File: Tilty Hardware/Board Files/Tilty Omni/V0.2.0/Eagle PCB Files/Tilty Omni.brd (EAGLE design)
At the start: 38.1 x 50.8 mm, 11 parts, among them U1 TEENSY_3.0_ALLPINS

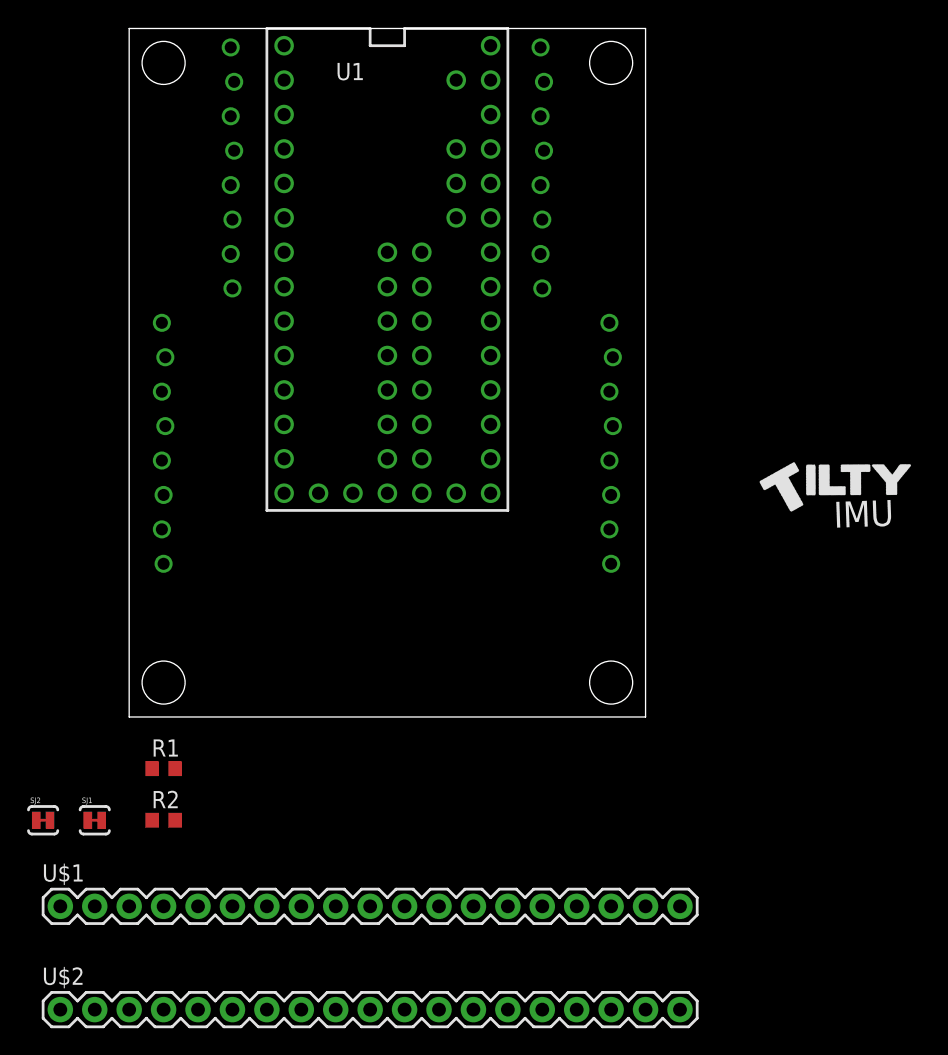
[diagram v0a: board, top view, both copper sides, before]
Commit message: Updated Tilty Omni pinout and removed Eagle backup files,as that's what GitHub is for
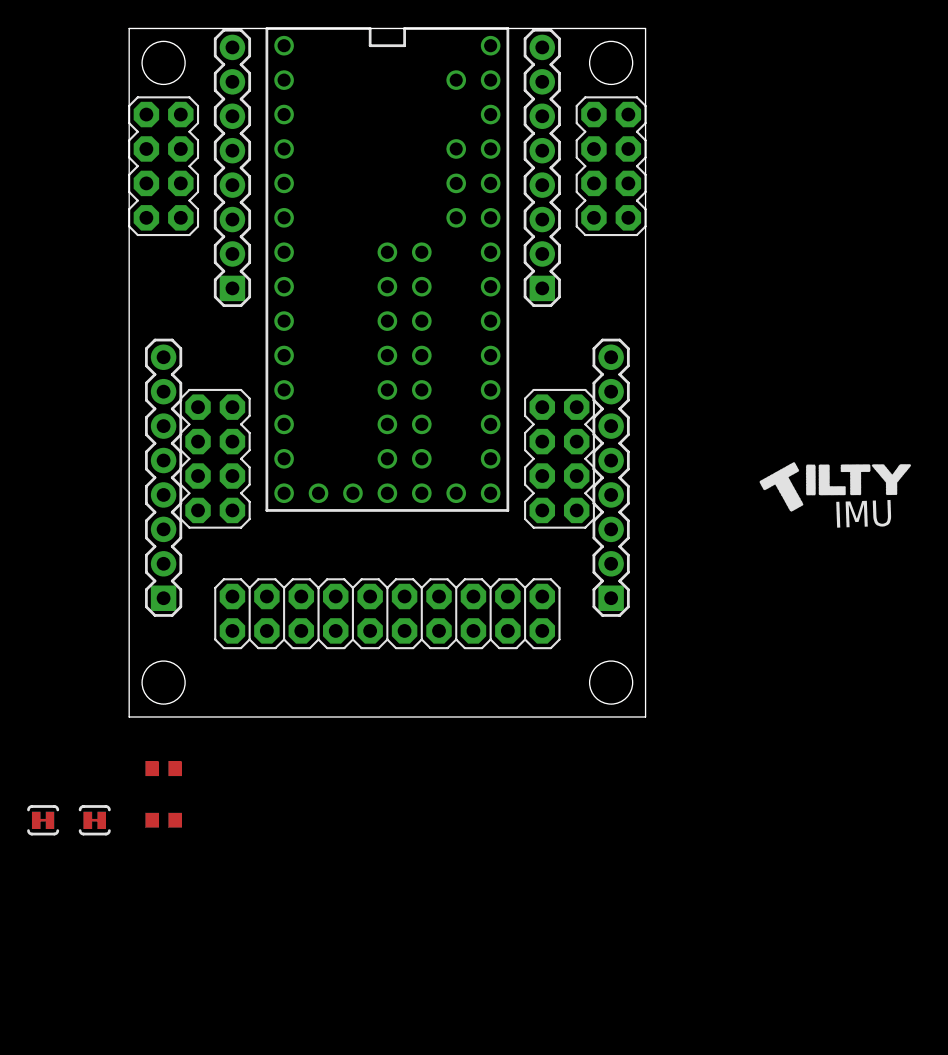
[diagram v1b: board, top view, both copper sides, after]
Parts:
- removed U$1, U$2: M191X19, SparkFun-Connectors:1X19
- added JP10: M10X2, SparkFun-Connectors:2X10
- added JP5, JP6, JP7, JP8: M04X2, SparkFun-Connectors:2X4
- JP1, JP2, JP3, JP4: value 8-PIN_HEADER -> (none); device My Parts:8-PIN_RECEPTACLE_LOCK_NO-SS -> SparkFun-Connectors:1X08
- moved JP2 11.4 mm to (2.54, 8.76), turned to 90 degrees
- moved JP3 11.4 mm to (35.6, 8.76), turned to 90 degrees
- moved JP1 8.89 mm to (7.62, 31.6), turned to 90 degrees
- moved JP4 8.89 mm to (30.5, 31.6), turned to 90 degrees
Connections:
- net N$14 renamed A13
- removed net N$1: U1.24
- removed net N$10: U1.33
- removed net N$2: U1.25
- removed net N$3: U1.26
- removed net N$4: U1.27
- removed net N$5: U1.28
- removed net N$6: U1.29
- removed net N$7: U1.30
- removed net N$8: U1.31
- removed net N$9: U1.32
- new net 24: JP10.10, U1.24
- new net 25: JP10.9, U1.25
- new net 26: JP10.8, U1.26
- new net 27: JP10.7, U1.27
- new net 28: JP10.6, U1.28
- new net 29: JP10.5, U1.29
- new net 30: JP10.4, U1.30
- new net 31: JP10.3, U1.31
- new net 32: JP10.2, U1.32
- new net 33: JP10.1, U1.33
- new net N$21: JP10.11
- new net N$22: JP10.13
- new net N$23: JP10.15
- new net N$24: JP10.17
- new net N$25: JP10.19
- new net N$31: JP10.12
- new net N$32: JP10.14
- new net N$33: JP10.16
- new net N$34: JP10.18
- new net N$35: JP10.20
- net +3V3: now also JP1.8, JP5.1; no longer JP1.P$1
- net +5V: now also JP4.8, JP8.2; no longer JP4.P$1
- net 10: now also JP2.5, JP6.4; no longer JP2.P$4
- net 20: now also JP4.3, JP8.5; no longer JP4.P$6
- net 21: now also JP4.4, JP8.6; no longer JP4.P$5
- net 3V_SCL: now also JP4.2, JP8.8; no longer JP4.P$7
- net 3V_SDA: now also JP4.1, JP8.7; no longer JP4.P$8
- net 5V_SCL: now also JP3.7, JP7.2; no longer JP3.P$2
- net 5V_SDA: now also JP3.8, JP7.1; no longer JP3.P$1
- net 7: now also JP2.8, JP6.1; no longer JP2.P$1
- net 8: now also JP2.7, JP6.2; no longer JP2.P$2
- net 9: now also JP2.6, JP6.3; no longer JP2.P$3
- net AUX_SCL: now also JP3.2, JP7.7; no longer JP3.P$7
- net AUX_SDA: now also JP3.3, JP7.6; no longer JP3.P$6
- net BATT_SENSE: now also JP3.5, JP7.4; no longer JP3.P$4
- net BLUETOOTH_RX: now also JP1.7, JP5.2; no longer JP1.P$2
- net BLUETOOTH_TX: now also JP1.6, JP5.3; no longer JP1.P$3
- net BT_CMD: now also JP3.6, JP7.3; no longer JP3.P$3
- net GND: now also JP2.1, JP3.1, JP4.7, JP6.8, JP7.8, JP8.1; no longer JP2.P$8, JP3.P$8, JP4.P$2
- net IMU_INT: now also JP1.2, JP5.7; no longer JP1.P$7
- net MEMORY_CS: now also JP1.1, JP5.8; no longer JP1.P$8
- net MISO: now also JP2.3, JP6.6; no longer JP2.P$6
- net MOSI: now also JP2.4, JP6.5; no longer JP2.P$5
- net SCK: now also JP3.4, JP7.5; no longer JP3.P$5
- net SERVO_1: now also JP1.5, JP5.4; no longer JP1.P$4
- net SERVO_2: now also JP1.4, JP5.5; no longer JP1.P$5
- net SERVO_3: now also JP4.5, JP8.4; no longer JP4.P$4
- net SERVO_4: now also JP4.6, JP8.3; no longer JP4.P$3
- net USB_CS: now also JP1.3, JP5.6; no longer JP1.P$6
- net VCC: now also JP2.2, JP6.7; no longer JP2.P$7

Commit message: Tilty Omni work
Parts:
- moved SJ2 59.9 mm to (15.2, 48.3)
- moved SJ1 58.5 mm to (24.1, 44.5)
- moved R2 30.5 mm to (24.1, 14.0)
- moved R1 28.5 mm to (26.7, 11.4)
- moved JP10 3.94 mm to (19.1, 3.68)
- moved JP7 1.53 mm to (31.1, 17.7)
- moved JP6 1.53 mm to (6.99, 17.7)
- moved JP8 0.65 mm to (34.9, 40.5)
- moved JP5 0.65 mm to (3.17, 40.5)
- moved U1 0.13 mm to (19.1, 32.9)
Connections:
- net N$21 renamed A12
- net N$22 renamed A10
- net N$32 renamed A11
- removed net N$23: JP10.15
- removed net N$24: JP10.17
- removed net N$25: JP10.19
- removed net N$31: JP10.12
- removed net N$33: JP10.16
- removed net N$34: JP10.18
- removed net N$35: JP10.20
- net +3V3: now also JP10.19
- net A13: now also JP10.12
- net AGND: now also JP10.16
- net AREF: now also JP10.15
- net GND: now also JP10.20
- net PGM: now also JP10.17
- net RESET: now also JP10.18
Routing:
- net 5V_SDA: track 0.00 -> 17.8 mm
- net 8: track 0.00 -> 14.4 mm
- net +5V: track 0.00 -> 13.6 mm
- net 9: track 0.00 -> 13.3 mm
- net 3V_SCL: track 0.00 -> 11.6 mm
- net 5V_SCL: track 0.00 -> 11.5 mm
- net 10: track 0.00 -> 11.5 mm
- net BT_CMD: track 0.00 -> 11.4 mm
- net SERVO_3: track 0.00 -> 11.3 mm
- net BLUETOOTH_TX: track 0.00 -> 10.8 mm
- net IMU_INT: track 0.00 -> 10.6 mm
- net SERVO_2: track 0.00 -> 10.6 mm
- net BATT_SENSE: track 0.00 -> 9.94 mm
- net SCK: track 0.00 -> 9.94 mm
- net MOSI: track 0.00 -> 9.94 mm
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
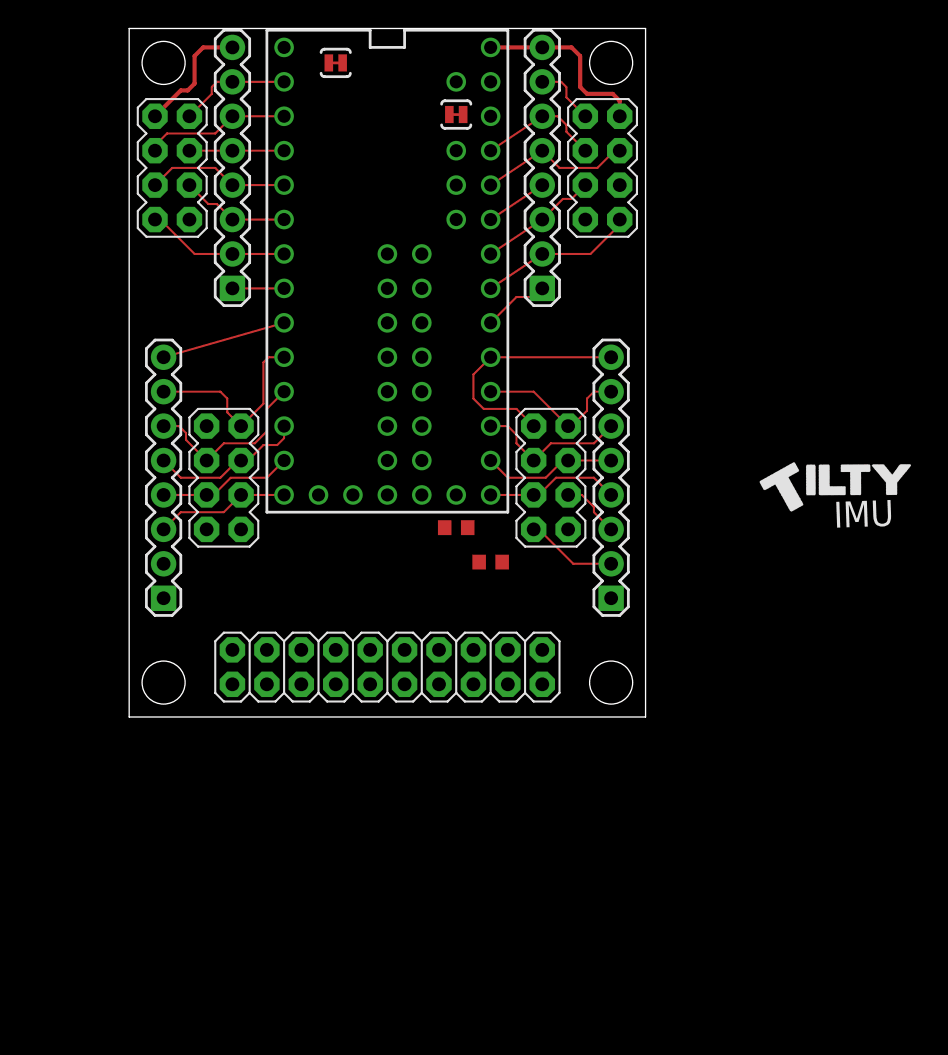
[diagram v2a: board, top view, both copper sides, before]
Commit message: Deleted redundant Tilty Omni backups
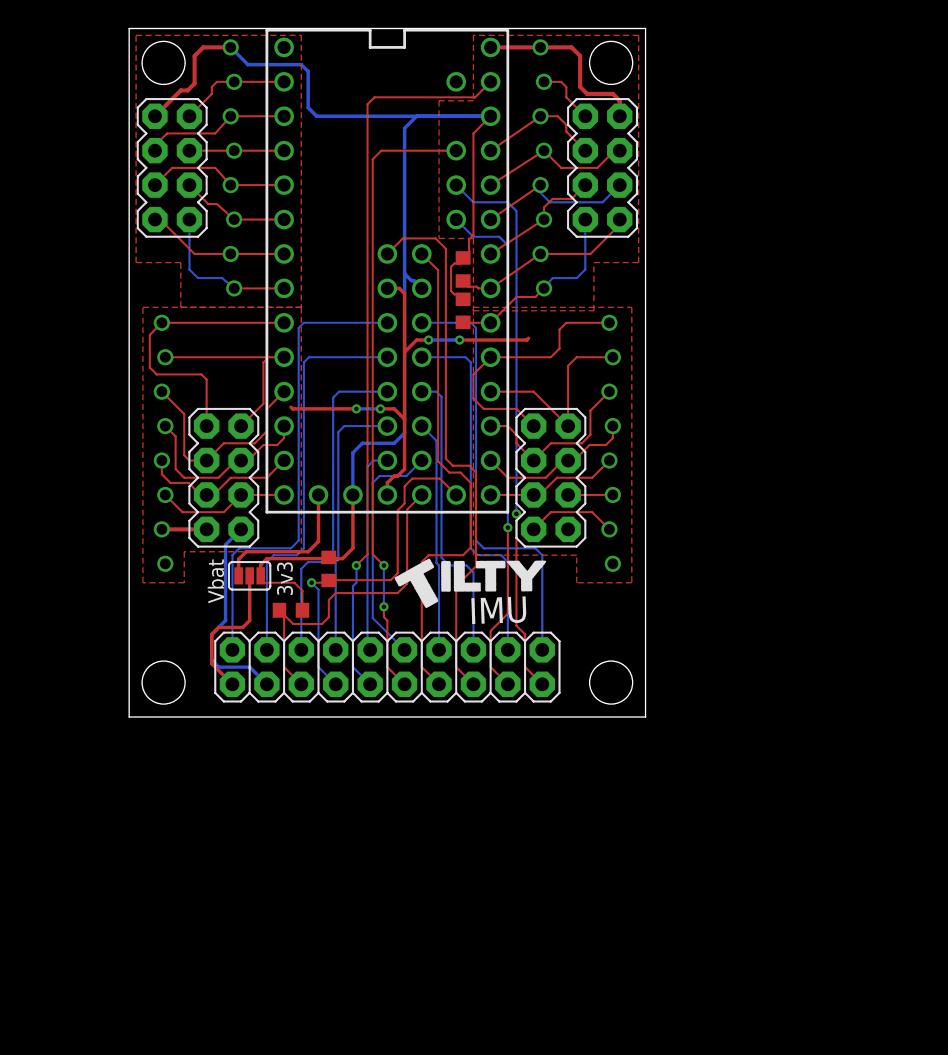
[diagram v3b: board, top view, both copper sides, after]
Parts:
- removed SJ1, SJ2: SOLDERJUMPERTRACE, SparkFun-Passives:SJ_2S-TRACE
- added R3, R4: 10k, resistor:R0603
- added SJ3: (no value), SparkFun-Passives:SJ_3_PASTE2&3
- JP1, JP2, JP3, JP4: value (none) -> 8-PIN_HEADER; device SparkFun-Connectors:1X08 -> My Parts:8-PIN_RECEPTACLE_LOCK_NO-SS
- moved R1 15.2 mm to (11.9, 7.87)
- moved JP2 11.4 mm to (2.54, 20.2)
- moved JP3 11.4 mm to (35.6, 20.2)
- moved R2 9.88 mm to (14.7, 10.9), turned to 90 degrees
- moved JP1 8.89 mm to (7.62, 40.5)
- moved JP4 8.89 mm to (30.5, 40.5)
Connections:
- removed net N$11: U1.A10
- removed net N$12: U1.A11
- removed net N$13: U1.A12
- removed net N$17: U1.VBAT
- new net N$2: JP10.1, SJ3.2
- new net VBAT: SJ3.1, U1.VBAT
- new net VUSB: U1.VUSB
- net +3V3: now also JP1.P$8, R3.2, R4.2, SJ3.3; no longer JP1.8, JP10.19, SJ2.2
- net +5V: now also JP4.P$8; no longer JP4.8, U1.VUSB
- net 10: now also JP2.P$5; no longer JP2.5
- net 20: now also JP4.P$3; no longer JP4.3
- net 21: now also JP4.P$4; no longer JP4.4
- net 24: now also JP10.2; no longer JP10.10
- net 25: now also JP10.4; no longer JP10.9
- net 26: now also JP10.6; no longer JP10.8
- net 27: now also JP10.8; no longer JP10.7
- net 28: now also JP10.10; no longer JP10.6
- net 29: now also JP10.12; no longer JP10.5
- net 30: now also JP10.14; no longer JP10.4
- net 31: now also JP10.16; no longer JP10.3
- net 32: now also JP10.18; no longer JP10.2
- net 33: now also JP10.20; no longer JP10.1
- net 3V_SCL: now also JP4.P$2, R3.1; no longer JP4.2
- net 3V_SDA: now also JP4.P$1, R4.1; no longer JP4.1
- net 5V_SCL: now also JP3.P$7; no longer JP3.7
- net 5V_SDA: now also JP3.P$8; no longer JP3.8
- net 7: now also JP2.P$8; no longer JP2.8
- net 8: now also JP2.P$7; no longer JP2.7
- net 9: now also JP2.P$6; no longer JP2.6
- net A10: now also JP10.19, U1.A10; no longer JP10.13
- net A11: now also JP10.17, U1.A11; no longer JP10.14
- net A12: now also JP10.15, U1.A12; no longer JP10.11
- net A13: now also JP10.13; no longer JP10.12
- net AGND: now also JP10.9; no longer JP10.16, SJ1.1
- net AREF: now also JP10.11; no longer JP10.15, SJ2.1
- net AUX_SCL: now also JP3.P$2; no longer JP3.2
- net AUX_SDA: now also JP3.P$3; no longer JP3.3
- net BATT_SENSE: now also JP3.P$5; no longer JP3.5
- net BLUETOOTH_RX: now also JP1.P$7; no longer JP1.7
- net BLUETOOTH_TX: now also JP1.P$6; no longer JP1.6
- net BT_CMD: now also JP3.P$6; no longer JP3.6
- net GND: now also JP10.3, JP2.P$1, JP3.P$1, JP4.P$7; no longer JP10.20, JP2.1, JP3.1, JP4.7, SJ1.2
- net IMU_INT: now also JP1.P$2; no longer JP1.2
- net MEMORY_CS: now also JP1.P$1; no longer JP1.1
- net MISO: now also JP2.P$3; no longer JP2.3
- net MOSI: now also JP2.P$4; no longer JP2.4
- net PGM: now also JP10.5; no longer JP10.17
- net RESET: now also JP10.7; no longer JP10.18
- net SCK: now also JP3.P$4; no longer JP3.4
- net SERVO_1: now also JP1.P$5; no longer JP1.5
- net SERVO_2: now also JP1.P$4; no longer JP1.4
- net SERVO_3: now also JP4.P$5; no longer JP4.5
- net SERVO_4: now also JP4.P$6; no longer JP4.6
- net USB_CS: now also JP1.P$3; no longer JP1.3
- net VCC: now also JP2.P$2; no longer JP2.2
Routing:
- net +3V3: track 9.01 -> 106.4 mm
- net AGND: track 0.00 -> 53.5 mm, vias 0 -> 1
- net GND: track 4.67 -> 55.2 mm, vias 0 -> 4
- net AREF: track 0.00 -> 46.1 mm, vias 0 -> 2
- net A10: track 0.00 -> 40.9 mm, vias 0 -> 1
- net A12: track 0.00 -> 40.0 mm
- net A11: track 0.00 -> 38.0 mm, vias 0 -> 1
- net A13: track 0.00 -> 37.2 mm
- net 24: track 0.00 -> 34.7 mm
- net 33: track 0.00 -> 32.2 mm
- net 25: track 0.00 -> 29.7 mm
- net 32: track 0.00 -> 27.1 mm
- net RESET: track 0.00 -> 26.0 mm, vias 0 -> 1
- net PGM: track 0.00 -> 24.9 mm
- net 26: track 0.00 -> 24.5 mm
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- added copper zone on layer 1, net GND
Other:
- board text added: "3v3"
- board text added: "Vbat"
